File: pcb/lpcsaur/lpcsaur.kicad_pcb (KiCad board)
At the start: 4 copper layers, 116.8 x 71.1 mm, 157 parts, among them IC1 74LV11, IC2 74LV10, IC3 74HCT08, IC4 74LVC07, IC5 74LVC07, IC6 LM1117-3.3, IC7 LPC1768_TQFP100, J1 X1, J10 LASER, J11 Motor X, J12 Motor Y, J13 Motor Z, J14 Motor AUX, J15 SSR, J16 SSR AUX, J17 RELAY1, J18 V-SELECT, J19 RELAY2, J2 X2, J20 V-SELECT, J21 USB_B, J22 RGB LED, J23 SERIAL, J24 5V IN, J25 12V IN, J26 24V IN, J27 AUX I/O, J28 CHILLER, J29 MICRO-SD, J3 Y1, J4 Y2, J5 Z1, J6 Z2, J7 DOOR1, J8 DOOR2, J9 E-STOP, Q1 ZXMN4A06, Q2 ZXMN4A06, Q3 BSL207SP, Q4 BSL207SP, SW1 SW_PUSH, SW2 SW_PUSH, SW3 ISP, X1 12 MHz

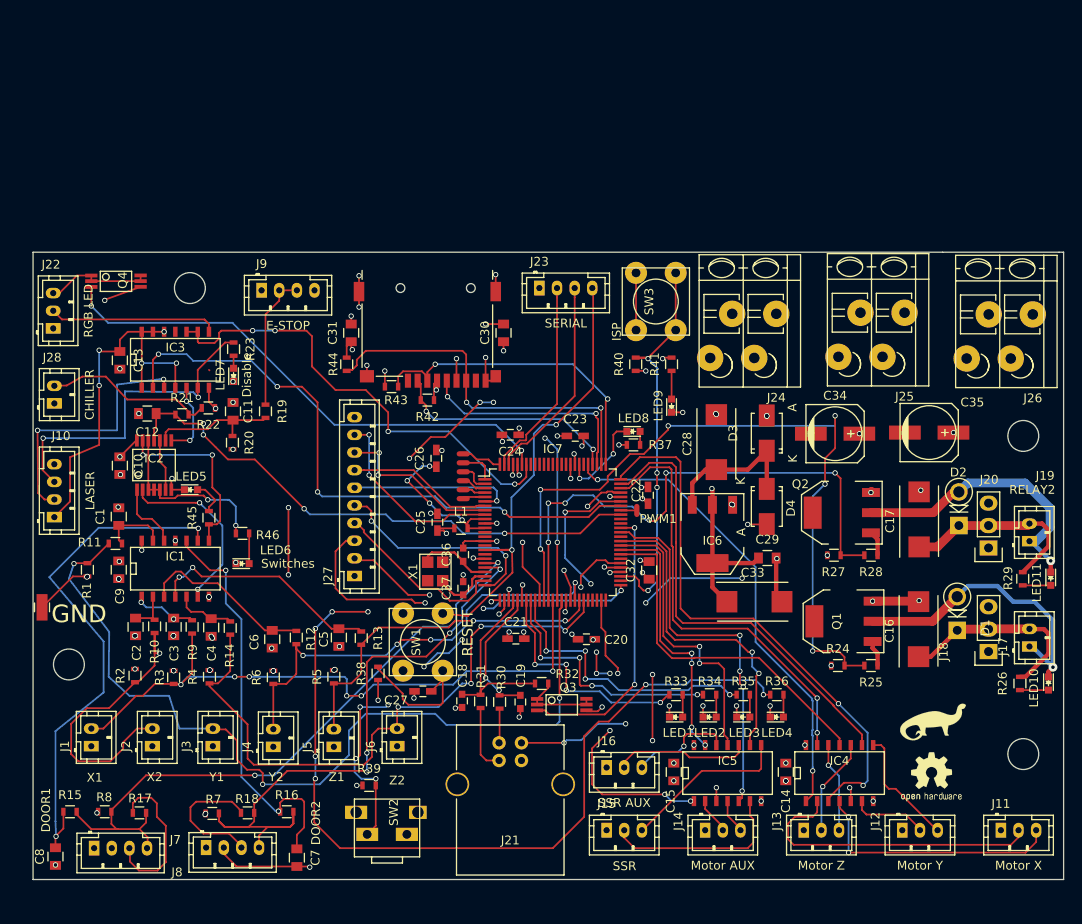
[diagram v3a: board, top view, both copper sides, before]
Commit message: Rename 10x10 to lpcsaur; delete original lpcsaur folder.
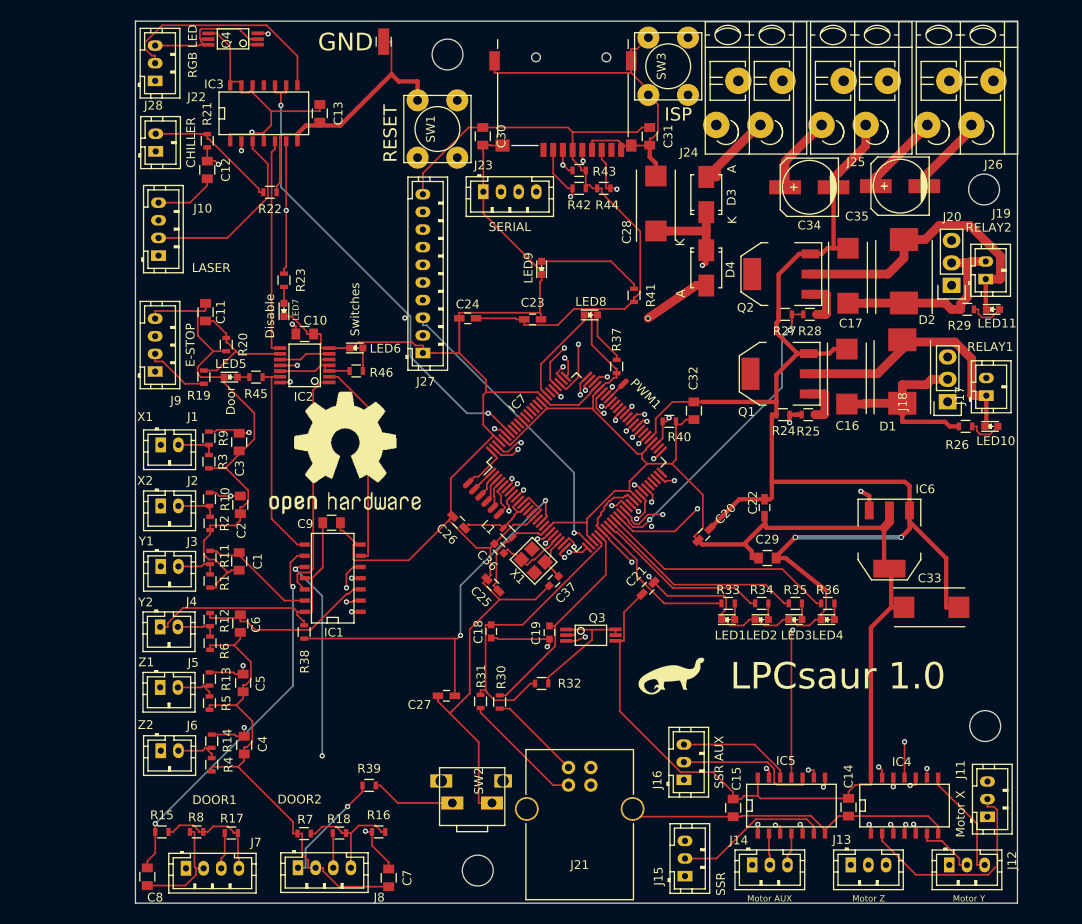
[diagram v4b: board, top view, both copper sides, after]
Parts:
- removed G***: LOGO, OPENHARDWARE:OSHWLOGO0.3IN
- removed G***: LOGO, lpcsaur:dino
- removed Hole1, Hole2, Hole3, Hole4: MountingHole_3.5mm, Mounting_Holes:MountingHole_3.5mm
- added G1: LOGO, lpcsaur:dino, F.Cu at (160.5, 124.1)
- added G2: LOGO, OPENHARDWARE:OSHWLOGO0.75IN, F.Cu at (114.2, 89.7)
- added HOLE1: MountingHole_3.5mm, Mounting_Holes:MountingHole_3.5mm, F.Cu at (196.2, 69.1)
- added HOLE2: MountingHole_3.5mm, Mounting_Holes:MountingHole_3.5mm, F.Cu at (196.3, 129.9)
- added HOLE3: MountingHole_3.5mm, Mounting_Holes:MountingHole_3.5mm, F.Cu at (138.8, 146.3)
- added HOLE4: MountingHole_3.5mm, Mounting_Holes:MountingHole_3.5mm, F.Cu at (135.4, 53.8)
- D1, D2: footprint Diodes_ThroughHole:Diode_DO-41_SOD81_Vertical_KathodeUp -> Diodes_SMD:DO-214AB
- SW3: value ISP -> SW_PUSH
- moved W1 74.9 mm to (128.1, 52.3)
- moved SW1 58.2 mm to (134.2, 62.2)
- moved C31 40.5 mm to (158.3, 63.1), turned to 270 degrees
- moved C13 36.0 mm to (120.9, 60.5)
- moved R44 35.3 mm to (153.1, 69.0), turned to 0 degrees
- moved J1 35.1 mm to (102.9, 98.0), turned to 0 degrees
- moved Q4 32.8 mm to (111.1, 50.7), turned to 90 degrees
- moved R43 32.5 mm to (150.3, 66.9), turned to 180 degrees
- moved J10 31.9 mm to (102.6, 76.6)
- moved LED11 31.2 mm to (197.2, 82.7), turned to 0 degrees
- moved R29 31.2 mm to (194.3, 82.7), turned to 0 degrees
- moved R21 31.2 mm to (108.1, 63.6), turned to 90 degrees
- moved J28 30.8 mm to (102.3, 64.8)
- moved J22 30.4 mm to (102.2, 56.8)
- moved J29 30.3 mm to (148.5, 54.1)
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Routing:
- net LED4: track 136.2 -> 27.3 mm, vias 8 -> 0
- net +3V3: track 400.7 -> 460.2 mm, vias 34 -> 3
- net P1.22: track 85.7 -> 27.5 mm, vias 6 -> 2
- net X-MAX: track 114.3 -> 56.4 mm, vias 8 -> 1
- net Y-MIN: track 98.2 -> 60.8 mm, vias 3 -> 1
- net GND: track 809.0 -> 845.6 mm, vias 88 -> 5
- net Z-MIN: track 39.5 -> 71.5 mm, vias 2 -> 1
- net Net-(C28-Pad1): track 16.8 -> 47.9 mm, vias 0 -> 2
- net P1.23: track 62.2 -> 35.6 mm, vias 6 -> 2
- net Net-(C3-Pad1): track 7.44 -> 31.2 mm
- net ~RESET: track 75.9 -> 99.2 mm
- net Net-(C4-Pad1): track 6.82 -> 28.9 mm, vias 0 -> 2
- net Net-(IC7-Pad8): track 19.2 -> 40.2 mm
- net +5V: track 259.1 -> 280.0 mm, vias 8 -> 1
- net Net-(C2-Pad1): track 4.40 -> 23.4 mm, vias 0 -> 2
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- removed copper zone on In1.Cu, net +3V3
- removed copper zone on In2.Cu, net GND
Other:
- board size 116.8 x 71.1 mm -> 100 x 100 mm
- board text added: "ISP"
- board text added: "LPCsaur 1.0"
